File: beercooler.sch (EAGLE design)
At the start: 17 parts, among them U1 ARDUINO_SHIELDLABEL

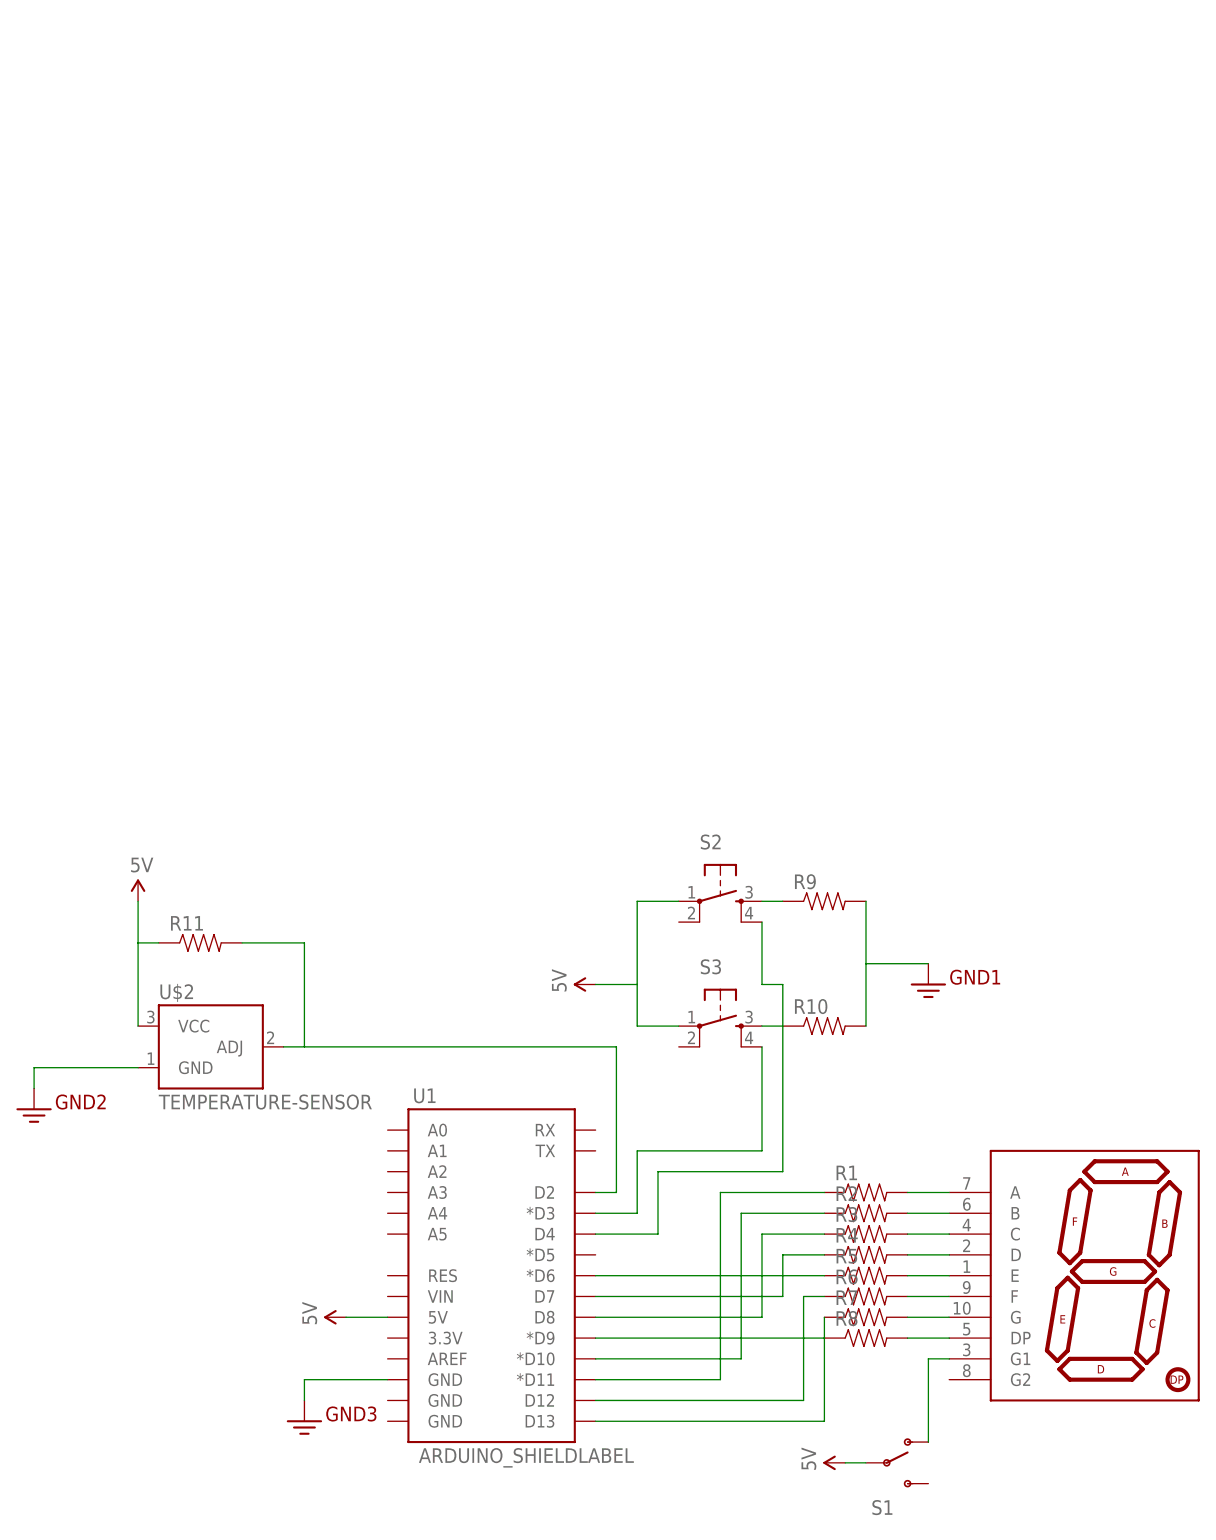
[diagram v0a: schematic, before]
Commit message: Updated eagle schema
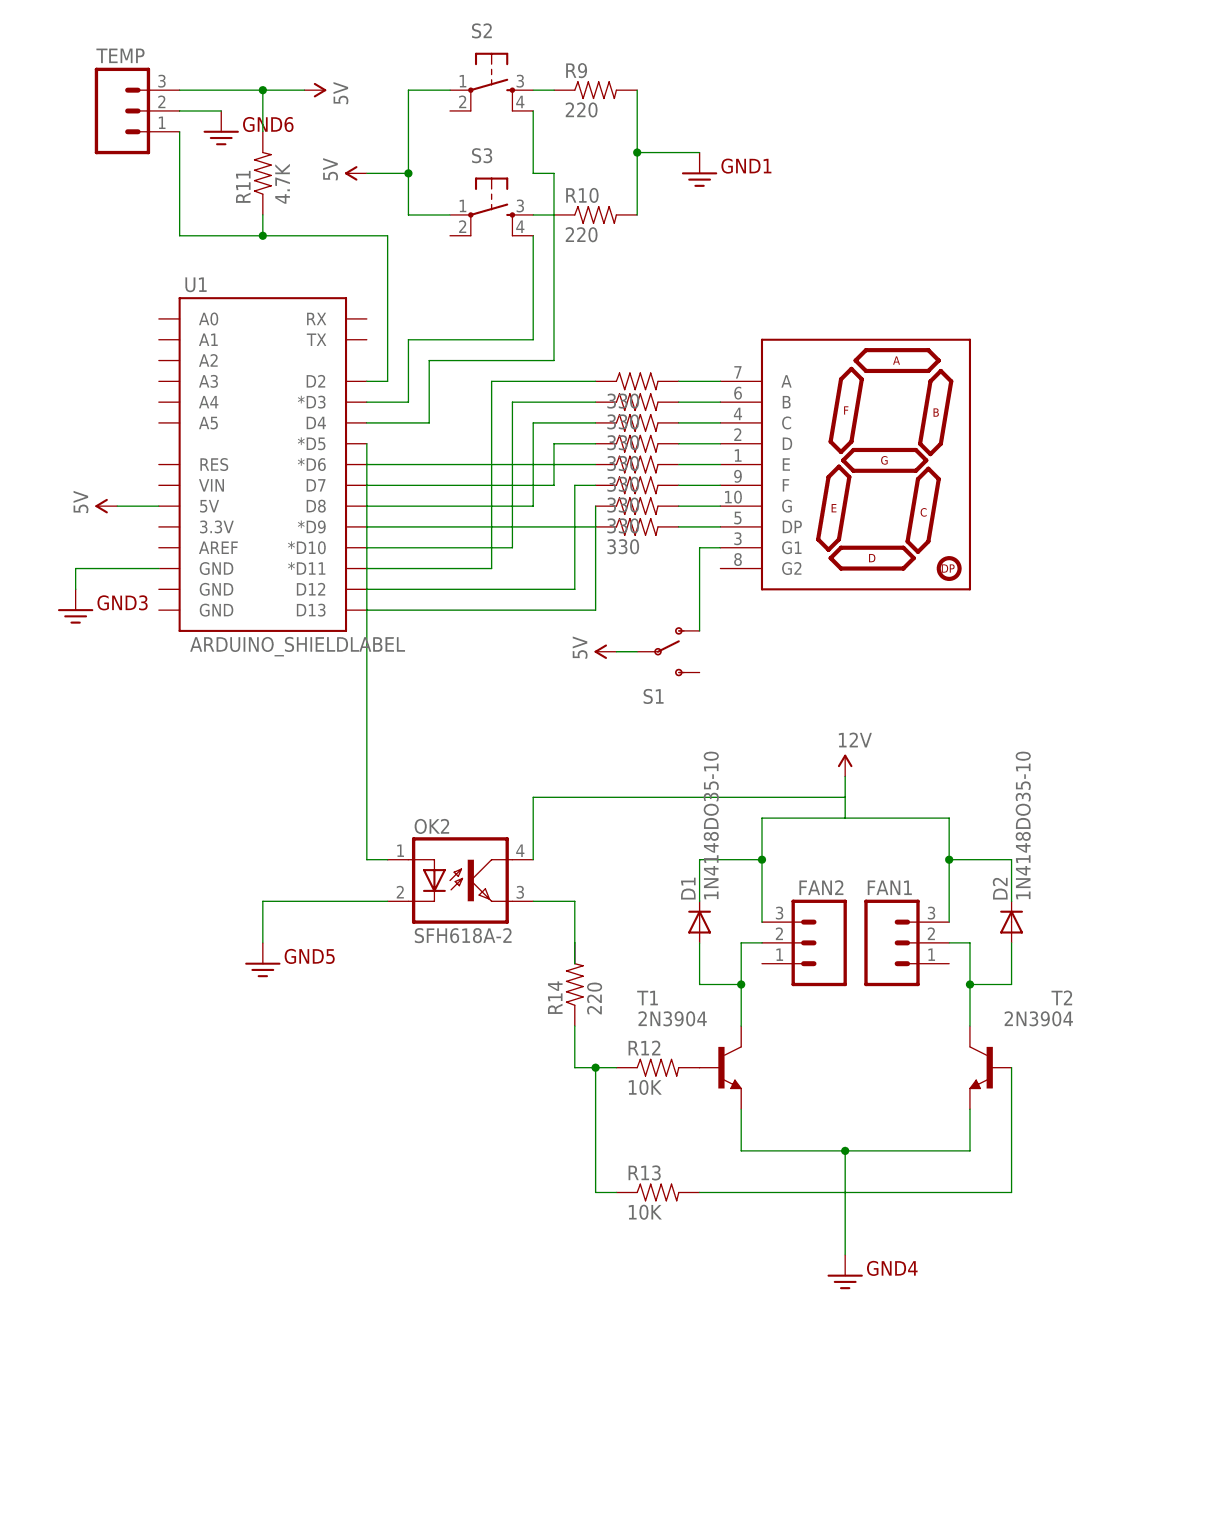
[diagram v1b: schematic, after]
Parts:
- removed U$2: TEMPERATURE-SENSOR, SparkFun-Sensors:TEMPERATURE-SENSOR
- added D1, D2: 1N4148DO35-10, diode:1N4148DO35-10
- added FAN1, FAN2, TEMP: (no value), SparkFun-Connectors:M03POLAR
- added OK2: SFH618A-2, optocoupler:SFH618A-2
- added R12, R13: 10K, SparkFun-Resistors:RESISTORPTH-1/4W
- added R14: 220, SparkFun-Resistors:RESISTORPTH-1/4W
- added T1, T2: 2N3904, transistor:2N3904
- R1, R2, R3, R4, R5, R6, R7, R8: value (none) -> 330
- R10, R9: value (none) -> 220
- R11: value (none) -> 4.7K
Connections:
- new net N$23: D2.A, FAN1.2
- new net N$25: OK2.A, U1.*D5
- new net N$26: D1.A, FAN2.2, T1.C
- new net N$27: R12.1, R13.1, R14.1
- new net N$28: R13.2, T2.B
- new net N$29: R12.2, T1.B
- new net N$31: OK2.EMIT, R14.2
- net 3.3V: now also D1.C, D2.C, FAN1.3, FAN2.3, OK2.C, OK2.COL, T1.E, T2.E, TEMP.2; no longer U$2.GND
- net 5V: now also R11.2, TEMP.3; no longer R11.1, U$2.VCC
- net N$24: now also R11.1; no longer R11.2, U$2.ADJ
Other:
- moved on the sheet: R10, R11, R9, S1, S2, S3, U1

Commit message: Added a missing resistor
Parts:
- added R15: 550, SparkFun-Resistors:RESISTORPTH-1/4W
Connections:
- new net N$32: OK2.A, R15.1
- net N$25: now also R15.2; no longer OK2.A
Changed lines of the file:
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@@
 <part name="SUPPLY6" library="SparkFun-Aesthetics" deviceset="5V" device=""/>
 <part name="GND6" library="SparkFun-Aesthetics" deviceset="GND2" device=""/>
+<part name="R15" library="SparkFun-Resistors" deviceset="RESISTOR" device="PTH-1/4W" value="550"/>
 </parts>
 <sheets>
@@
 <instance part="SUPPLY6" gate="G$1" x="40.64" y="187.96" rot="R270"/>
 <instance part="GND6" gate="G$1" x="30.48" y="182.88"/>
+<instance part="R15" gate="G$1" x="48.26" y="106.68" rot="R90"/>
 </instances>
 <busses>
@@
 <net name="N$25" class="0">
 <segment>
-<pinref part="OK2" gate="G$1" pin="A"/>
 <pinref part="U1" gate="G$1" pin="*D5"/>
-<wire x1="50.8" y1="93.98" x2="48.26" y2="93.98" width="0.1524" layer="91"/>
-<wire x1="48.26" y1="93.98" x2="48.26" y2="144.78" width="0.1524" layer="91"/>
+<pinref part="R15" gate="G$1" pin="2"/>
+<wire x1="48.26" y1="111.76" x2="48.26" y2="144.78" width="0.1524" layer="91"/>
 </segment>
 </net>
@@
 </segment>
 </net>
+<net name="N$32" class="0">
+<segment>
+<pinref part="OK2" gate="G$1" pin="A"/>
+<wire x1="50.8" y1="93.98" x2="48.26" y2="93.98" width="0.1524" layer="91"/>
+<wire x1="48.26" y1="93.98" x2="48.26" y2="101.6" width="0.1524" layer="91"/>
+<pinref part="R15" gate="G$1" pin="1"/>
+</segment>
+</net>

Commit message: Changed pins following soldering and fixed schematic
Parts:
- removed R15: 550, SparkFun-Resistors:RESISTORPTH-1/4W
- R1, R2, R3, R4, R5, R6, R7, R8: value 330 -> 680
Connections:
- removed net N$32: OK2.A, R15.1
- net N$25: now also R14.2; no longer R15.2
- net N$27: now also OK2.A; no longer R12.1, R13.1
- net N$31: now also R12.1, R13.1; no longer R14.2
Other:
- moved on the sheet: R14
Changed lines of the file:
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@@
 </classes>
 <parts>
-<part name="R1" library="SparkFun-Resistors" deviceset="RESISTOR" device="PTH-1/4W" value="330"/>
-<part name="R2" library="SparkFun-Resistors" deviceset="RESISTOR" device="PTH-1/4W" value="330"/>
-<part name="R3" library="SparkFun-Resistors" deviceset="RESISTOR" device="PTH-1/4W" value="330"/>
-<part name="R4" library="SparkFun-Resistors" deviceset="RESISTOR" device="PTH-1/4W" value="330"/>
-<part name="R5" library="SparkFun-Resistors" deviceset="RESISTOR" device="PTH-1/4W" value="330"/>
-<part name="R6" library="SparkFun-Resistors" deviceset="RESISTOR" device="PTH-1/4W" value="330"/>
-<part name="R7" library="SparkFun-Resistors" deviceset="RESISTOR" device="PTH-1/4W" value="330"/>
-<part name="R8" library="SparkFun-Resistors" deviceset="RESISTOR" device="PTH-1/4W" value="330"/>
+<part name="R1" library="SparkFun-Resistors" deviceset="RESISTOR" device="PTH-1/4W" value="680"/>
+<part name="R2" library="SparkFun-Resistors" deviceset="RESISTOR" device="PTH-1/4W" value="680"/>
+<part name="R3" library="SparkFun-Resistors" deviceset="RESISTOR" device="PTH-1/4W" value="680"/>
+<part name="R4" library="SparkFun-Resistors" deviceset="RESISTOR" device="PTH-1/4W" value="680"/>
+<part name="R5" library="SparkFun-Resistors" deviceset="RESISTOR" device="PTH-1/4W" value="680"/>
+<part name="R6" library="SparkFun-Resistors" deviceset="RESISTOR" device="PTH-1/4W" value="680"/>
+<part name="R7" library="SparkFun-Resistors" deviceset="RESISTOR" device="PTH-1/4W" value="680"/>
+<part name="R8" library="SparkFun-Resistors" deviceset="RESISTOR" device="PTH-1/4W" value="680"/>
 <part name="R9" library="SparkFun-Resistors" deviceset="RESISTOR" device="PTH-1/4W" value="220"/>
 <part name="R10" library="SparkFun-Resistors" deviceset="RESISTOR" device="PTH-1/4W" value="220"/>
@@
 <part name="SUPPLY6" library="SparkFun-Aesthetics" deviceset="5V" device=""/>
 <part name="GND6" library="SparkFun-Aesthetics" deviceset="GND2" device=""/>
-<part name="R15" library="SparkFun-Resistors" deviceset="RESISTOR" device="PTH-1/4W" value="550"/>
 </parts>
 <sheets>
@@
 <instance part="R12" gate="G$1" x="83.82" y="68.58"/>
 <instance part="R13" gate="G$1" x="83.82" y="53.34"/>
-<instance part="R14" gate="G$1" x="73.66" y="78.74" rot="R90"/>
+<instance part="R14" gate="G$1" x="48.26" y="104.14" rot="R90"/>
 <instance part="FAN1" gate="G$1" x="111.76" y="83.82"/>
 <instance part="FAN2" gate="G$1" x="104.14" y="83.82" rot="MR0"/>
@@
 <instance part="SUPPLY6" gate="G$1" x="40.64" y="187.96" rot="R270"/>
 <instance part="GND6" gate="G$1" x="30.48" y="182.88"/>
-<instance part="R15" gate="G$1" x="48.26" y="106.68" rot="R90"/>
 </instances>
 <busses>
@@
 <segment>
 <pinref part="U1" gate="G$1" pin="*D5"/>
-<pinref part="R15" gate="G$1" pin="2"/>
-<wire x1="48.26" y1="111.76" x2="48.26" y2="144.78" width="0.1524" layer="91"/>
-</segment>
-</net>
-<net name="N$27" class="0">
-<segment>
-<wire x1="73.66" y1="68.58" x2="76.2" y2="68.58" width="0.1524" layer="91"/>
+<pinref part="R14" gate="G$1" pin="2"/>
+<wire x1="48.26" y1="109.22" x2="48.26" y2="144.78" width="0.1524" layer="91"/>
+</segment>
+</net>
+<net name="N$28" class="0">
+<segment>
+<pinref part="T2" gate="G1" pin="B"/>
+<wire x1="127" y1="53.34" x2="127" y2="68.58" width="0.1524" layer="91"/>
+<pinref part="R13" gate="G$1" pin="2"/>
+<wire x1="88.9" y1="53.34" x2="127" y2="53.34" width="0.1524" layer="91"/>
+</segment>
+</net>
+<net name="N$29" class="0">
+<segment>
+<pinref part="T1" gate="G1" pin="B"/>
+<pinref part="R12" gate="G$1" pin="2"/>
+</segment>
+</net>
+<net name="N$31" class="0">
+<segment>
+<pinref part="OK2" gate="G$1" pin="EMIT"/>
+<wire x1="68.58" y1="88.9" x2="76.2" y2="88.9" width="0.1524" layer="91"/>
 <wire x1="76.2" y1="68.58" x2="76.2" y2="53.34" width="0.1524" layer="91"/>
 <pinref part="R12" gate="G$1" pin="1"/>
@@
 <wire x1="76.2" y1="53.34" x2="78.74" y2="53.34" width="0.1524" layer="91"/>
 <junction x="76.2" y="68.58"/>
+<wire x1="76.2" y1="88.9" x2="76.2" y2="68.58" width="0.1524" layer="91"/>
+</segment>
+</net>
+<net name="N$27" class="0">
+<segment>
 <pinref part="R14" gate="G$1" pin="1"/>
-<wire x1="73.66" y1="68.58" x2="73.66" y2="73.66" width="0.1524" layer="91"/>
-</segment>
-</net>
-<net name="N$28" class="0">
-<segment>
-<pinref part="T2" gate="G1" pin="B"/>
-<wire x1="127" y1="53.34" x2="127" y2="68.58" width="0.1524" layer="91"/>
-<pinref part="R13" gate="G$1" pin="2"/>
-<wire x1="88.9" y1="53.34" x2="127" y2="53.34" width="0.1524" layer="91"/>
-</segment>
-</net>
-<net name="N$29" class="0">
-<segment>
-<pinref part="T1" gate="G1" pin="B"/>
-<pinref part="R12" gate="G$1" pin="2"/>
-</segment>
-</net>
-<net name="N$31" class="0">
-<segment>
-<pinref part="OK2" gate="G$1" pin="EMIT"/>
-<wire x1="68.58" y1="88.9" x2="73.66" y2="88.9" width="0.1524" layer="91"/>
-<pinref part="R14" gate="G$1" pin="2"/>
-<wire x1="73.66" y1="88.9" x2="73.66" y2="83.82" width="0.1524" layer="91"/>
-<wire x1="73.66" y1="83.82" x2="73.66" y2="81.28" width="0.1524" layer="91"/>
-</segment>
-</net>
-<net name="N$32" class="0">
-<segment>
 <pinref part="OK2" gate="G$1" pin="A"/>
 <wire x1="50.8" y1="93.98" x2="48.26" y2="93.98" width="0.1524" layer="91"/>
-<wire x1="48.26" y1="93.98" x2="48.26" y2="101.6" width="0.1524" layer="91"/>
-<pinref part="R15" gate="G$1" pin="1"/>
-</segment>
-</net>
+<wire x1="48.26" y1="93.98" x2="48.26" y2="99.06" width="0.1524" layer="91"/>
+</segment>
+</net>

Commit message: Removed a switch
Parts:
- removed S1: (no value), SparkFun-Electromechanical:SWITCH-SPDT-SMD-A
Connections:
- removed net N$22: S1.O, U$1.G1
- net 5V: now also U$1.G1; no longer S1.P
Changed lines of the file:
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@@
 <part name="U1" library="SparkFun-Boards" deviceset="ARDUINO_SHIELD" device="LABEL"/>
 <part name="U$1" library="SparkFun-Displays" deviceset="7-SEGMENT-DISPLAY-1&quot;-RED" device=""/>
-<part name="S1" library="SparkFun-Electromechanical" deviceset="SWITCH-SPDT" device="-SMD-A"/>
 <part name="S2" library="SparkFun-Electromechanical" deviceset="TAC_SWITCH" device="PTH"/>
 <part name="GND1" library="SparkFun-Aesthetics" deviceset="GND2" device=""/>
@@
 <instance part="U1" gate="G$1" x="35.56" y="142.24"/>
 <instance part="U$1" gate="G$1" x="111.76" y="142.24"/>
-<instance part="S1" gate="1" x="83.82" y="119.38"/>
 <instance part="S2" gate="S" x="63.5" y="187.96"/>
 <instance part="GND1" gate="G$1" x="88.9" y="177.8"/>
@@
 <segment>
 <pinref part="SUPPLY1" gate="G$1" pin="5V"/>
-<pinref part="S1" gate="1" pin="P"/>
-<wire x1="78.74" y1="119.38" x2="81.28" y2="119.38" width="0.1524" layer="91"/>
+<wire x1="88.9" y1="119.38" x2="88.9" y2="132.08" width="0.1524" layer="91"/>
+<pinref part="U$1" gate="G$1" pin="G1"/>
+<wire x1="88.9" y1="132.08" x2="91.44" y2="132.08" width="0.1524" layer="91"/>
+<wire x1="78.74" y1="119.38" x2="88.9" y2="119.38" width="0.1524" layer="91"/>
 </segment>
 <segment>
@@
 </segment>
 </net>
-<net name="N$22" class="0">
-<segment>
-<pinref part="S1" gate="1" pin="O"/>
-<wire x1="88.9" y1="121.92" x2="88.9" y2="132.08" width="0.1524" layer="91"/>
-<pinref part="U$1" gate="G$1" pin="G1"/>
-<wire x1="88.9" y1="132.08" x2="91.44" y2="132.08" width="0.1524" layer="91"/>
-</segment>
-</net>
